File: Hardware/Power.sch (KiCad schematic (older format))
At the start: 22 parts, among them P301 USB_B, P302 CONN_01X02, U301 MCP1700T-3302E/TT_, U302 FT232RQ

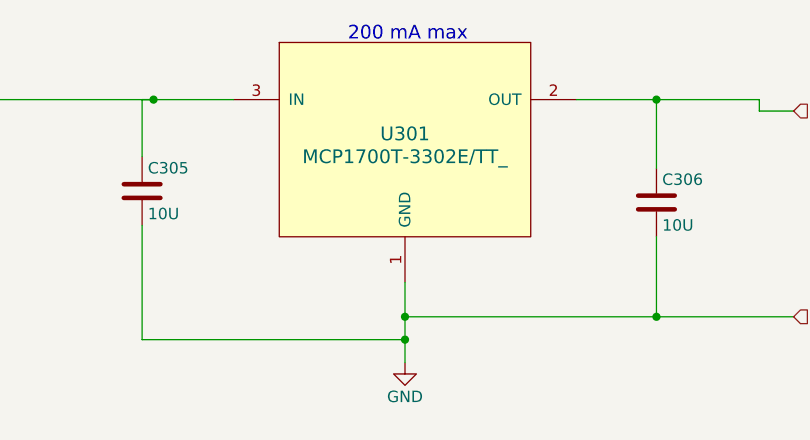
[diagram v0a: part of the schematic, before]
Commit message: Rename project files to remove the space between 'Central' & 'Command' for the XSL processing of the BOM
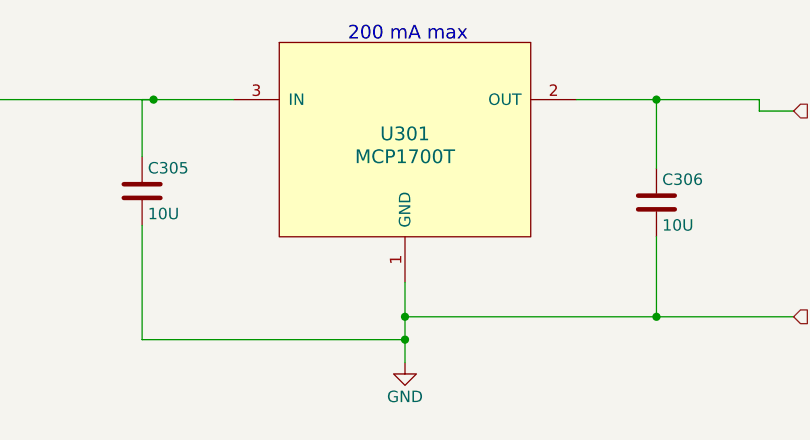
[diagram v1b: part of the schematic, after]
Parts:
- D301, D302: Link (none) -> http://parts.io/detail/305034/B130-13-F; MPN (none) -> B130-13-F
- P301: Link (none) -> http://parts.io/detail/93261255/10118193-0001LF; MPN (none) -> 10118193
- U301: value MCP1700T-3302E/TT_ -> MCP1700T; MPN (none) -> MCP1700T-3302E/TT_
- U302: Link (none) -> http://parts.io/detail/3622205/FT232RQ-REEL; MPN (none) -> FT232RQ-REEL
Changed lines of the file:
@@
 EESchema Schematic File Version 2
-LIBS:Central Command-rescue
 LIBS:power
 LIBS:device
@@
 LIBS:valves
 LIBS:stm32f030c8
-LIBS:Central Command-cache
+LIBS:CentralCommand-cache
 EELAYER 25 0
 EELAYER END
@@
 P 5500 1100
 F 0 "U301" H 5500 1100 60  0000 C CNN
-F 1 "MCP1700T-3302E/TT_" H 5500 1000 60  0000 C CNN
+F 1 "MCP1700T" H 5500 1000 60  0000 C CNN
 F 2 "Housings_SOT-23_SOT-143_TSOT-6:SOT-23" H 5500 1100 60  0001 C CNN
 F 3 "" H 5500 1100 60  0000 C CNN
-F 4 "http://parts.io/detail/1370896/MCP1700T-3302E%2FTT" H 5500 1100 60  0001 C CNN "Link"
+F 4 "MCP1700T-3302E/TT_" H 5500 1100 60  0001 C CNN "MPN"
+F 5 "http://parts.io/detail/1370896/MCP1700T-3302E%2FTT" H 5500 1100 60  0001 C CNN "Link"
 	1    5500 1100
 	1    0    0    -1
@@
 $EndComp
 $Comp
-L GND #PWR010
+L GND #PWR09
 U 1 1 56441AA8
 P 5500 2100
-F 0 "#PWR010" H 5500 1850 50  0001 C CNN
+F 0 "#PWR09" H 5500 1850 50  0001 C CNN
 F 1 "GND" H 5500 1950 50  0000 C CNN
 F 2 "" H 5500 2100 60  0000 C CNN
@@
 $EndComp
 $Comp
-L GND #PWR011
+L GND #PWR010
 U 1 1 56442E32
 P 2550 1600
-F 0 "#PWR011" H 2550 1350 50  0001 C CNN
+F 0 "#PWR010" H 2550 1350 50  0001 C CNN
 F 1 "GND" H 2550 1450 50  0000 C CNN
 F 2 "" H 2550 1600 60  0000 C CNN
@@
 F 2 "Housings_DFN_QFN:QFN-32-1EP_5x5mm_Pitch0.5mm" H 7700 4900 60  0001 C CNN
 F 3 "" H 7700 4900 60  0000 C CNN
+F 4 "FT232RQ-REEL" H 5550 4750 60  0001 C CNN "MPN"
+F 5 "http://parts.io/detail/3622205/FT232RQ-REEL" H 5550 4750 60  0001 C CNN "Link"
 	1    5550 4750
 	1    0    0    -1
@@
 F 2 "CentralCommand:10118193" V 1150 3100 60  0001 C CNN
 F 3 "" V 1150 3100 60  0000 C CNN
+F 4 "10118193" H 1200 3200 60  0001 C CNN "MPN"
+F 5 "http://parts.io/detail/93261255/10118193-0001LF" H 1200 3200 60  0001 C CNN "Link"
 	1    1200 3200
 	-1   0    0    -1
@@
 $EndComp
 $Comp
-L GND #PWR012
+L GND #PWR011
 U 1 1 565615CA
 P 1100 4750
-F 0 "#PWR012" H 1100 4500 50  0001 C CNN
+F 0 "#PWR011" H 1100 4500 50  0001 C CNN
 F 1 "GND" H 1100 4600 50  0000 C CNN
 F 2 "" H 1100 4750 60  0000 C CNN
@@
 F 2 "Diodes_SMD:Diode-SMA_Standard" H 3100 950 60  0001 C CNN
 F 3 "" H 3100 950 60  0000 C CNN
+F 4 "B130-13-F" H 3100 950 60  0001 C CNN "MPN"
+F 5 "http://parts.io/detail/305034/B130-13-F" H 3100 950 60  0001 C CNN "Link"
 	1    3100 950
 	-1   0    0    1
@@
 F 2 "Diodes_SMD:Diode-SMA_Standard" H 3700 2650 60  0001 C CNN
 F 3 "" H 3700 2650 60  0000 C CNN
+F 4 "B130-13-F" H 3700 2650 60  0001 C CNN "MPN"
+F 5 "http://parts.io/detail/305034/B130-13-F" H 3700 2650 60  0001 C CNN "Link"
 	1    3700 2650
 	0    1    1    0
@@
 $EndComp
 $Comp
-L GND #PWR013
+L GND #PWR012
 U 1 1 56568175
 P 3550 6150
-F 0 "#PWR013" H 3550 5900 50  0001 C CNN
+F 0 "#PWR012" H 3550 5900 50  0001 C CNN
 F 1 "GND" H 3550 6000 50  0000 C CNN
 F 2 "" H 3550 6150 60  0000 C CNN
@@
 $EndComp
 $Comp
-L GND #PWR014
+L GND #PWR013
 U 1 1 5656A044
 P 5350 6250
-F 0 "#PWR014" H 5350 6000 50  0001 C CNN
+F 0 "#PWR013" H 5350 6000 50  0001 C CNN
 F 1 "GND" H 5350 6100 50  0000 C CNN
 F 2 "" H 5350 6250 60  0000 C CNN
@@
 $EndComp
 $Comp
-L GND #PWR015
+L GND #PWR014
 U 1 1 5656D2A7
 P 7300 4450
-F 0 "#PWR015" H 7300 4200 50  0001 C CNN
+F 0 "#PWR014" H 7300 4200 50  0001 C CNN
 F 1 "GND" H 7300 4300 50  0000 C CNN
 F 2 "" H 7300 4450 60  0000 C CNN

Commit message: - Added Farnell and digi-key supplier numbers to most past. Still need todo crystal, switch and micro inductor. - updated the HTML BOM and CSV
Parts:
- C301, C302, C304: Farnell (none) -> 2496944; MPN (none) -> 0805B104K500CT
- C303: Farnell (none) -> 1845775; MPN (none) -> GRM32RR71C475KA01L
- C305, C306: Farnell (none) -> 9227989; MPN (none) -> C1210C106Z4VACTU
- D301, D302: Farnell (none) -> 1843713
- D303, D304: Farnell (none) -> 2062259; MPN (none) -> SML-LXT0805GW-TR
- L301: Farnell (none) -> 1800342; MPN (none) -> 742792605
- P301: Digi-Key (none) -> 609-4616-1-ND; Farnell (none) -> 2506569
- P302: Farnell (none) -> 1022247; MPN (none) -> M20-9990246
- R301, R302, R303: Farnell (none) -> 9333681; MPN (none) -> MC01W08050R
- R306, R307: Farnell (none) -> 2447618; MPN (none) -> MCWR08X2700FTL
- U301: Farnell (none) -> 1296592
- U302: Farnell (none) -> 1146033
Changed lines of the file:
@@
 F 4 "MCP1700T-3302E/TT_" H 5500 1100 60  0001 C CNN "MPN"
 F 5 "http://parts.io/detail/1370896/MCP1700T-3302E%2FTT" H 5500 1100 60  0001 C CNN "Link"
+F 6 "1296592" H 5500 1100 60  0001 C CNN "Farnell"
 	1    5500 1100
 	1    0    0    -1
@@
 F 2 "Capacitors_SMD:C_1210" H 4388 1200 30  0001 C CNN
 F 3 "" H 4350 1350 60  0000 C CNN
+F 4 "	9227989" H 4350 1350 60  0001 C CNN "Farnell"
+F 5 "C1210C106Z4VACTU" H 4350 1350 60  0001 C CNN "MPN"
 	1    4350 1350
 	1    0    0    -1
@@
 F 2 "Capacitors_SMD:C_1210" H 6638 1250 30  0001 C CNN
 F 3 "" H 6600 1400 60  0000 C CNN
+F 4 "9227989" H 6600 1400 60  0001 C CNN "Farnell"
+F 5 "C1210C106Z4VACTU" H 6600 1400 60  0001 C CNN "MPN"
 	1    6600 1400
 	1    0    0    -1
@@
 F 2 "Pin_Headers:Pin_Header_Straight_1x02" H 1950 1000 60  0001 C CNN
 F 3 "" H 1950 1000 60  0000 C CNN
+F 4 "1022247" H 1950 1000 60  0001 C CNN "Farnell"
+F 5 "M20-9990246" H 1950 1000 60  0001 C CNN "MPN"
 	1    1950 1000
 	-1   0    0    -1
@@
 F 4 "FT232RQ-REEL" H 5550 4750 60  0001 C CNN "MPN"
 F 5 "http://parts.io/detail/3622205/FT232RQ-REEL" H 5550 4750 60  0001 C CNN "Link"
+F 6 "1146033" H 5550 4750 60  0001 C CNN "Farnell"
 	1    5550 4750
 	1    0    0    -1
@@
 F 4 "10118193" H 1200 3200 60  0001 C CNN "MPN"
 F 5 "http://parts.io/detail/93261255/10118193-0001LF" H 1200 3200 60  0001 C CNN "Link"
+F 6 "609-4616-1-ND" H 1200 3200 60  0001 C CNN "Digi-Key"
+F 7 "2506569" H 1200 3200 60  0001 C CNN "Farnell"
 	1    1200 3200
 	-1   0    0    -1
@@
 F 2 "Inductors_NEOSID:Neosid_Inductor_SM1206" H 3250 3650 60  0001 C CNN
 F 3 "" H 3250 3650 60  0000 C CNN
+F 4 "1800342" V 3250 3650 60  0001 C CNN "Farnell"
+F 5 "742792605" V 3250 3650 60  0001 C CNN "MPN"
 	1    3250 3650
 	0    -1   -1   0
@@
 F 2 "Capacitors_SMD:C_0805" H 2488 4250 30  0001 C CNN
 F 3 "" H 2450 4400 60  0000 C CNN
+F 4 "2496944" H 2450 4400 60  0001 C CNN "Farnell"
+F 5 "0805B104K500CT" H 2450 4400 60  0001 C CNN "MPN"
 	1    2450 4400
 	1    0    0    -1
@@
 F 4 "B130-13-F" H 3100 950 60  0001 C CNN "MPN"
 F 5 "http://parts.io/detail/305034/B130-13-F" H 3100 950 60  0001 C CNN "Link"
+F 6 "1843713" H 3100 950 60  0001 C CNN "Farnell"
 	1    3100 950
 	-1   0    0    1
@@
 F 4 "B130-13-F" H 3700 2650 60  0001 C CNN "MPN"
 F 5 "http://parts.io/detail/305034/B130-13-F" H 3700 2650 60  0001 C CNN "Link"
+F 6 "1843713" H 3700 2650 60  0001 C CNN "Farnell"
 	1    3700 2650
 	0    1    1    0
@@
 F 2 "Capacitors_SMD:C_1210" H 3738 5450 30  0001 C CNN
 F 3 "" H 3700 5600 60  0000 C CNN
+F 4 "1845775" H 3700 5600 60  0001 C CNN "Farnell"
+F 5 "GRM32RR71C475KA01L" H 3700 5600 60  0001 C CNN "MPN"
 	1    3700 5600
 	1    0    0    -1
@@
 F 2 "Capacitors_SMD:C_0805" H 3388 5450 30  0001 C CNN
 F 3 "" H 3350 5600 60  0000 C CNN
+F 4 "2496944" H 3350 5600 60  0001 C CNN "Farnell"
+F 5 "0805B104K500CT" H 3350 5600 60  0001 C CNN "MPN"
 	1    3350 5600
 	1    0    0    -1
@@
 F 2 "Capacitors_SMD:C_0805" H 4188 5650 30  0001 C CNN
 F 3 "" H 4150 5800 60  0000 C CNN
+F 4 "2496944" H 4150 5800 60  0001 C CNN "Farnell"
+F 5 "0805B104K500CT" H 4150 5800 60  0001 C CNN "MPN"
 	1    4150 5800
 	1    0    0    -1
@@
 F 2 "Resistors_SMD:R_0805" V 4180 5000 30  0001 C CNN
 F 3 "" H 4250 5000 30  0000 C CNN
+F 4 "9333681" V 4250 5000 60  0001 C CNN "Farnell"
+F 5 "MC01W08050R" V 4250 5000 60  0001 C CNN "MPN"
 	1    4250 5000
 	0    1    1    0
@@
 F 2 "Resistors_SMD:R_0805" V 8330 4100 30  0001 C CNN
 F 3 "" H 8400 4100 30  0000 C CNN
+F 4 "2447618" V 8400 4100 60  0001 C CNN "Farnell"
+F 5 "MCWR08X2700FTL" V 8400 4100 60  0001 C CNN "MPN"
 	1    8400 4100
 	1    0    0    -1
@@
 F 2 "LEDs:LED-0805" H 8400 4600 60  0001 C CNN
 F 3 "" H 8400 4600 60  0000 C CNN
+F 4 "2062259" H 8400 4600 60  0001 C CNN "Farnell"
+F 5 "SML-LXT0805GW-TR" H 8400 4600 60  0001 C CNN "MPN"
 	1    8400 4600
 	0    -1   -1   0
@@
 F 2 "Resistors_SMD:R_0805" V 8680 4100 30  0001 C CNN
 F 3 "" H 8750 4100 30  0000 C CNN
+F 4 "2447618" V 8750 4100 60  0001 C CNN "Farnell"
+F 5 "MCWR08X2700FTL" V 8750 4100 60  0001 C CNN "MPN"
 	1    8750 4100
 	1    0    0    -1
@@
 F 2 "LEDs:LED-0805" H 8750 4600 60  0001 C CNN
 F 3 "" H 8750 4600 60  0000 C CNN
+F 4 "2062259" H 8750 4600 60  0001 C CNN "Farnell"
+F 5 "SML-LXT0805GW-TR" H 8750 4600 60  0001 C CNN "MPN"
 	1    8750 4600
 	0    -1   -1   0
@@
 F 2 "Resistors_SMD:R_0805" V 6830 3750 30  0001 C CNN
 F 3 "" H 6900 3750 30  0000 C CNN
+F 4 "9333681" V 6900 3750 60  0001 C CNN "Farnell"
+F 5 "MC01W08050R" V 6900 3750 60  0001 C CNN "MPN"
 	1    6900 3750
 	0    1    1    0
@@
 F 2 "Resistors_SMD:R_0805" V 6830 3900 30  0001 C CNN
 F 3 "" H 6900 3900 30  0000 C CNN
+F 4 "9333681" V 6900 3900 60  0001 C CNN "Farnell"
+F 5 "MC01W08050R" V 6900 3900 60  0001 C CNN "MPN"
 	1    6900 3900
 	0    1    1    0

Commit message: minor farnell number correction
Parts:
- C305: Farnell 9227989 -> 9227989
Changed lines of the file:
@@
 F 2 "Capacitors_SMD:C_1210" H 4388 1200 30  0001 C CNN
 F 3 "" H 4350 1350 60  0000 C CNN
-F 4 "	9227989" H 4350 1350 60  0001 C CNN "Farnell"
+F 4 "9227989" H 4350 1350 60  0001 C CNN "Farnell"
 F 5 "C1210C106Z4VACTU" H 4350 1350 60  0001 C CNN "MPN"
 	1    4350 1350

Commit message: Fixed the seed studion connect farnell code. It now points to the 2mm version
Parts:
- P301: Farnell 2506569 -> 2443115; MPN 10118193 -> 10118193 or USB3075-30-A
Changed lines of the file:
@@
 F 2 "CentralCommand:10118193" V 1150 3100 60  0001 C CNN
 F 3 "" V 1150 3100 60  0000 C CNN
-F 4 "10118193" H 1200 3200 60  0001 C CNN "MPN"
+F 4 "10118193 or USB3075-30-A" H 1200 3200 60  0001 C CNN "MPN"
 F 5 "http://parts.io/detail/93261255/10118193-0001LF" H 1200 3200 60  0001 C CNN "Link"
 F 6 "609-4616-1-ND" H 1200 3200 60  0001 C CNN "Digi-Key"
-F 7 "2506569" H 1200 3200 60  0001 C CNN "Farnell"
+F 7 "2443115" H 1200 3200 60  0001 C CNN "Farnell"
 	1    1200 3200
 	-1   0    0    -1
